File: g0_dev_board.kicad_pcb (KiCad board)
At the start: 4 copper layers, 80 x 114 mm, 198 parts, among them J201 USB_B_Mini, J202 F103_SWD, J301 USB_B_Mini, J401 RJ45_Hanrun_HR911105A_Horizon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, J501 DM3AT-SF-PEJM5, J801 Uno_IOH, J802 Uno_IOL, J803 Uno_POWER, J804 Uno_ANALOG, J805 J_LA_L, J806 J_LA_R, Q201 MMBT3904, SW701 RESET, SW702 USER, U101 STM32G0B1CCT6, U201 USBLC6-2SC6, U202 AP7361C-33E, U203 STM32F103CBTx, U301 USBLC6-2SC6, U302 FT232RL, U401 W5500, U501 W25Q32JVSSIQ, U601 TMP100, U602 TMP100, Y101 32.768kHz CL7pF, Y201 8MHz, Y401 25MHz

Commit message: feat(pcb): prepare board for placement
- Зелёные LED остаются C2297 (InGaN), резисторы к ним 330 Ом (C17630):
  ток 0.6-2.1 мА при Vf 2.6-3.1 В. Жёлто-зелёные отклонены: по
  даташитам световая отдача на мА у них в ~10 раз ниже.
- Цепи дифпар переименованы, чтобы KiCad распознавал пары:
  J201_D+/-, STL_D+/-, FT_D+/-, RXI_P/N; шаблоны классов USB90/MDI100
  обновлены.
- Отверстия шилда H801-H804: footprint из шаблона Arduino (NPTH 3.2,
  courtyard 3.4) в проектной библиотеке g0_dev_board.pretty вместо M3
  с courtyard 6.9, конфликтовавшего с разъёмами Uno.
- Исправлена арифметика в комментарии к двухцветному LED ST-Link.
- Плата синхронизирована со схемой: паритет 0, нарушений DRC 0.
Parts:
- D203, D401, D402, D403, D404: value YELLOW-GREEN -> LED
- D302: value YELLOW-GREEN -> TX
- D303: value YELLOW-GREEN -> RX
- H801, H802, H803, H804: value MountingHole_3.2mm_M3 -> Arduino_MountingHole_3.2mm; footprint MountingHole:MountingHole_3.2mm_M3 -> g0_dev_board:Arduino_MountingHole_3.2mm
- LD701: value YELLOW-GREEN -> GREEN
- R203, R424, R425, R426, R427: value 470 -> 330
- R306, R307, R701: value 390 -> 330
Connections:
- net /ft232rl/USB_DM renamed /ft232rl/FT_D-
- net /ft232rl/USB_DP renamed /ft232rl/FT_D+
- net /st_link/DM_J1 renamed /st_link/J201_D-
- net /st_link/DP_J1 renamed /st_link/J201_D+
- net /st_link/USB_DM renamed /st_link/STL_D-
- net /st_link/USB_DP renamed /st_link/STL_D+
- net /w5500/RXNNET renamed /w5500/RXI_N
- net /w5500/RXPNET renamed /w5500/RXI_P

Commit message: feat(pcb): draft component placement
Черновая расстановка по эскизу E (контрольная точка перед ручной
правкой в GUI):
- сверху вне зоны шилда: USB J201/J301, перемычки JP801/JP101/JP201,
  J202, кнопки, светодиоды; снизу: RJ45 J401 и microSD J501 на кромке,
  светодиоды W5500;
- под шилдом: ST-Link слева сверху, FT232 справа сверху, LDO по центру
  с медью под табом, U101 в центре (сторона SPI2/USART1/SWD к W5500),
  W5500 над RJ45, флэш и подтяжки SD на шине SPI2, TMP100 у МК и у LDO;
- развязка 100n <= 1.9 мм от выводов питания, высоты под шилдом <= 8 мм,
  полосы подписей гребёнок свободны.

Взвешенная длина ratsnest уменьшена на 6.7% итерациями. DRC: 0
нарушений, паритет 0, неразведённых связей 499.
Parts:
- moved D403 286.2 mm to (114.6, 139.2), turned to 90 degrees
- moved D402 283.4 mm to (114.6, 143.1), turned to 90 degrees
- moved D401 280.7 mm to (114.6, 147.0), turned to 90 degrees
- moved R424 275.4 mm to (117.5, 143.0), turned to -90 degrees
- moved R414 265.1 mm to (122.5, 115.5)
- moved R403 264.6 mm to (126.5, 115.5)
- moved R402 258.6 mm to (127.5, 112.5), turned to 90 degrees
- moved C407 258.6 mm to (126.0, 123.5), turned to -90 degrees
- moved R413 258.4 mm to (123.5, 107.0)
- moved C410 256.4 mm to (140.7, 120.5), turned to -90 degrees
- moved R430 255.0 mm to (120.0, 142.5), turned to 90 degrees
- moved R412 252.4 mm to (125.5, 109.5)
- moved C408 251.7 mm to (137.5, 122.7)
- moved R401 251.2 mm to (130.0, 109.5)
- moved R411 250.6 mm to (124.5, 118.0)
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
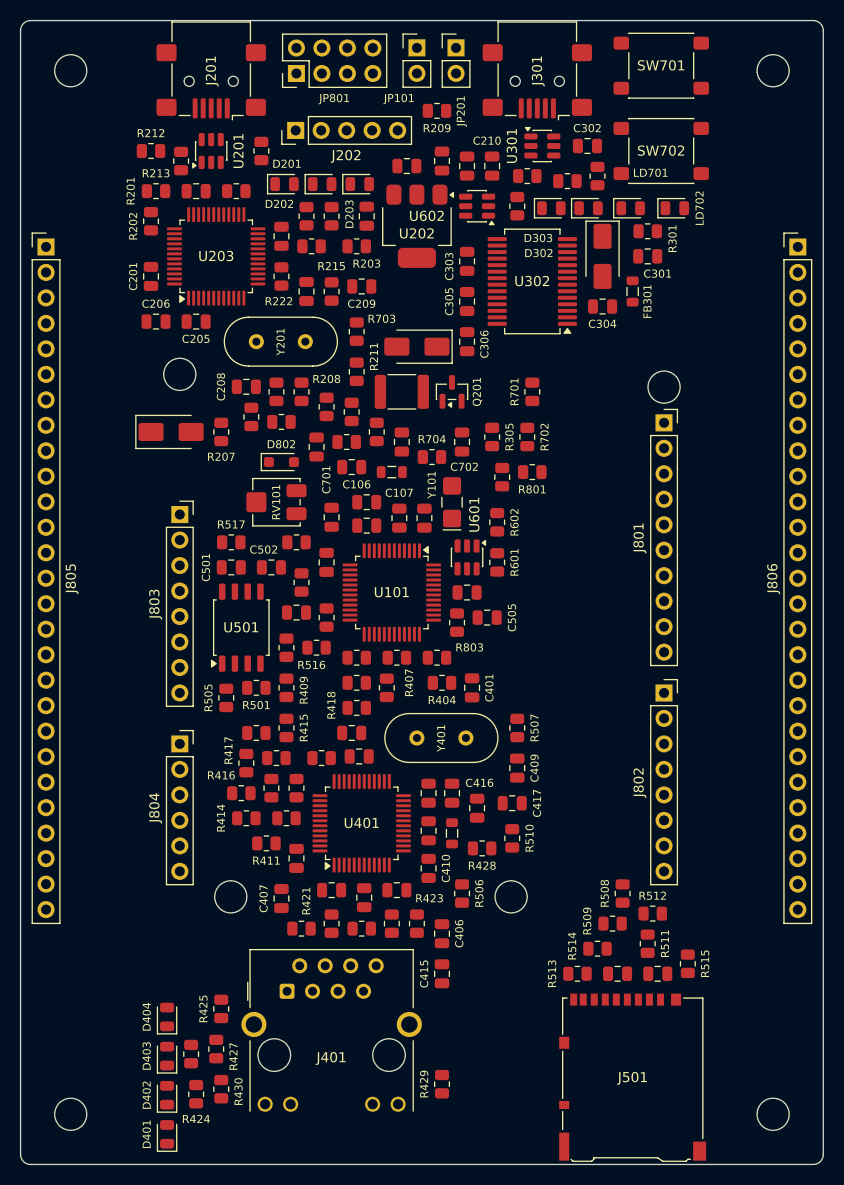
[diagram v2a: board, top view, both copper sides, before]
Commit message: feat(pcb): refine placement, add ground planes and route critical nets
Расстановка доработана: кварцы Y101/Y201/Y401 вплотную к выводам, терминация MDI
в линию между W5500 и RJ45, U203 повёрнут на 180°, флэш перенесён к microSD.
In1.Cu и In2.Cu — сплошная GND, на внешних слоях заливка GND, ~500 переходных
прошивки. Разведены и заблокированы: USB-пары (выровнены), MDI, кварцы, силовой
тракт и развязка, SPI2, USART1, SWD до JP801. DRC: 0 ошибок, паритет схемы полный,
208 неразведённых связей оставлены автотрассировщику.
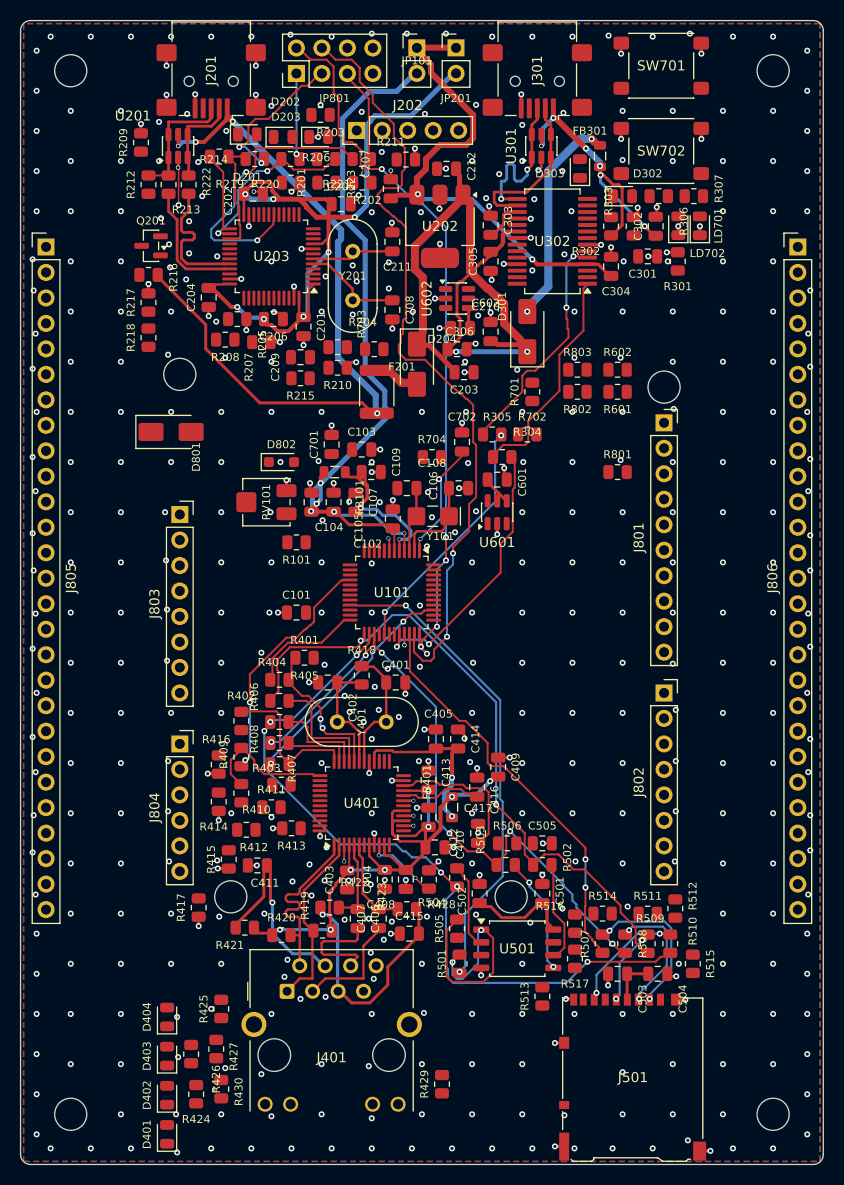
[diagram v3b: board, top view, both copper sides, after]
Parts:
- moved R517 53.8 mm to (155.2, 129.5), turned to 90 degrees
- moved C501 44.9 mm to (152.0, 123.0), turned to 90 degrees
- moved U501 42.2 mm to (149.5, 128.5), turned to 0 degrees
- moved R516 39.8 mm to (155.2, 126.0), turned to 90 degrees
- moved C502 38.6 mm to (145.8, 123.0), turned to 90 degrees
- moved R501 34.2 mm to (143.8, 130.0), turned to 90 degrees
- moved R802 33.4 mm to (155.5, 73.0), turned to 0 degrees
- moved Q201 33.3 mm to (113.0, 58.5), turned to 180 degrees
- moved R502 32.7 mm to (152.0, 120.2), turned to 0 degrees
- moved R505 32.5 mm to (143.5, 126.5)
- moved R209 29.7 mm to (112.0, 48.1), turned to 90 degrees
- moved R503 28.7 mm to (148.3, 120.2), turned to 0 degrees
- moved R803 27.9 mm to (155.5, 70.8), turned to 0 degrees
- moved R217 26.2 mm to (112.8, 64.1)
- moved R504 24.1 mm to (143.5, 121.4), turned to 90 degrees
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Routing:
- net /MCU_SWDIO: track 0.00 -> 77.7 mm, vias 0 -> 2
- net /SPI2_MISO: track 0.00 -> 73.1 mm, vias 0 -> 6
- net +3V3_MCU: track 0.00 -> 72.5 mm, vias 0 -> 5
- net /MCU_SWCLK: track 0.00 -> 71.8 mm, vias 0 -> 6
- net +3V3_STL: track 0.00 -> 70.6 mm, vias 0 -> 7
- net /st_link/VBUS_STL: track 0.00 -> 70.1 mm, vias 0 -> 4
- net +3.3V: track 0.00 -> 69.0 mm, vias 0 -> 4
- net /SPI2_SCK: track 0.00 -> 64.4 mm, vias 0 -> 2
- net /SPI2_MOSI: track 0.00 -> 61.9 mm, vias 0 -> 6
- net +5V: track 0.00 -> 61.3 mm, vias 0 -> 2
- net GND: track 0.00 -> 54.9 mm, vias 0 -> 507
- net /w5500/3V3A: track 0.00 -> 48.8 mm, vias 0 -> 8
- net /FL_CS: track 0.00 -> 47.1 mm, vias 0 -> 2
- net /SD_CS: track 0.00 -> 39.5 mm, vias 0 -> 2
- net /st_link/STL_NRST: track 0.00 -> 27.6 mm, vias 0 -> 2
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- added copper zone on B.Cu, net GND
- added copper zone on F.Cu, net GND
- added copper zone on In1.Cu, net GND
- added copper zone on In2.Cu, net GND

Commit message: refactor(pcb): remove routing and ground zones for manual re-routing
Удалены все дорожки и переходные (1555) и зоны GND на F/In1/In2/B по решению
перейти на ручную трассировку через MCP. Доработанная расстановка из 6c14ea2
сохранена. DRC: паритет со схемой полный, 499 неразведённых связей.
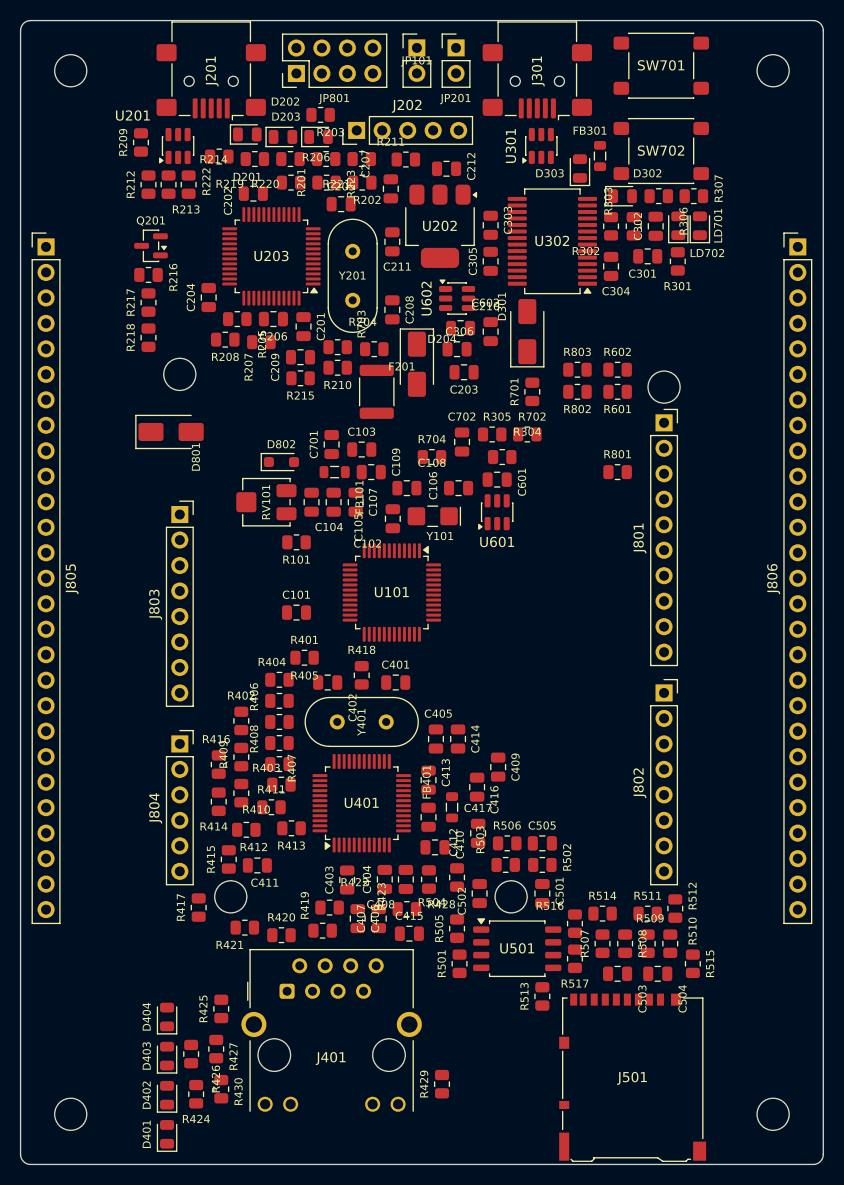
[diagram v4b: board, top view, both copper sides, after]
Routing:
- net /MCU_SWDIO: track 77.7 -> 0.00 mm, vias 2 -> 0
- net /SPI2_MISO: track 73.1 -> 0.00 mm, vias 6 -> 0
- net +3V3_MCU: track 72.5 -> 0.00 mm, vias 5 -> 0
- net /MCU_SWCLK: track 71.8 -> 0.00 mm, vias 6 -> 0
- net +3V3_STL: track 70.6 -> 0.00 mm, vias 7 -> 0
- net /st_link/VBUS_STL: track 70.1 -> 0.00 mm, vias 4 -> 0
- net +3.3V: track 69.0 -> 0.00 mm, vias 4 -> 0
- net /SPI2_SCK: track 64.4 -> 0.00 mm, vias 2 -> 0
- net /SPI2_MOSI: track 61.9 -> 0.00 mm, vias 6 -> 0
- net +5V: track 61.3 -> 0.00 mm, vias 2 -> 0
- net GND: track 54.9 -> 0.00 mm, vias 507 -> 0
- net /w5500/3V3A: track 48.8 -> 0.00 mm, vias 8 -> 0
- net /FL_CS: track 47.1 -> 0.00 mm, vias 2 -> 0
- net /SD_CS: track 39.5 -> 0.00 mm, vias 2 -> 0
- net /st_link/STL_NRST: track 27.6 -> 0.00 mm, vias 2 -> 0
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- removed copper zone on B.Cu, net GND
- removed copper zone on F.Cu, net GND
- removed copper zone on In1.Cu, net GND
- removed copper zone on In2.Cu, net GND

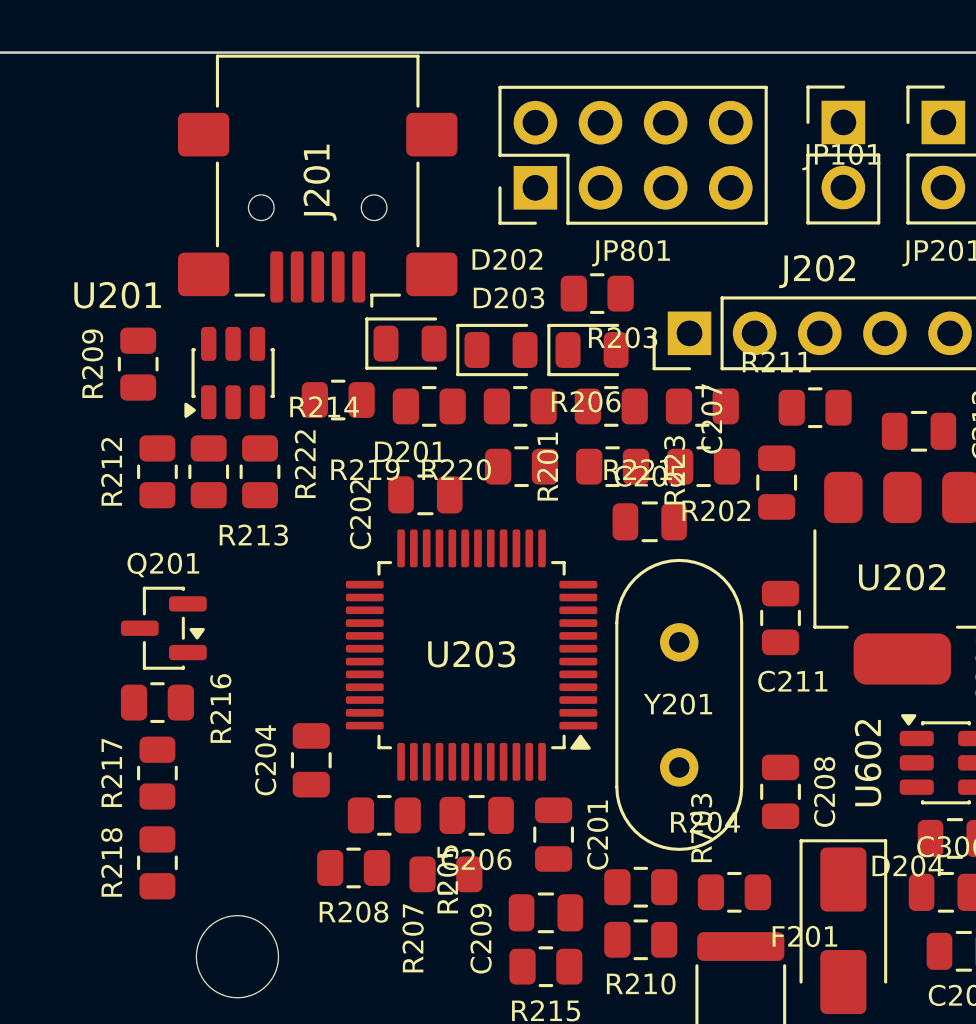
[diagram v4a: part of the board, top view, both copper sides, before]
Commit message: feat(pcb): manually route ST-Link USB, SWD and F103 escapes
Ручная трассировка через MCP: USB-пара J201 -> USBLC6 -> 0R -> F103, SWD-цепи
к JP801, верхний ряд выводов F103 (PA5, NRST, BOOT1), LED, SWO, SWD самого F103
к J202. Плоскости GND на In1/In2 восстановлены. R222 и C204 повёрнуты, C202
сдвинут на 0.4 мм ради каналов. Добавлен .kicad_dru: зазор внутри дифпар
USB 0.15 мм и MDI 0.18 мм. DRC: 0 нарушений.
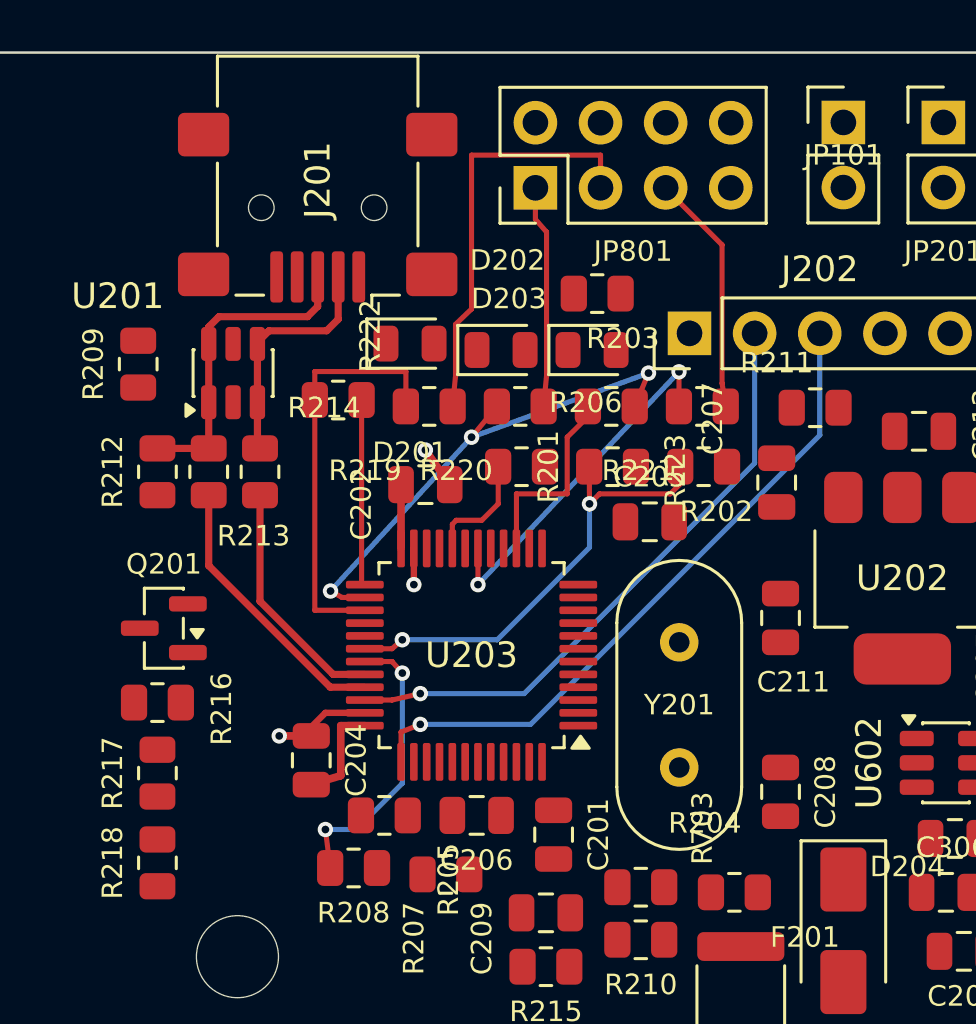
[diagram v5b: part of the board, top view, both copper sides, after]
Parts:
- moved C202 0.40 mm to (123.2, 52.9)
- turned C204 to 90 degrees
- turned R222 to 180 degrees
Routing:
- net /st_link/F103_SWCLK: track 0.00 -> 26.2 mm, vias 0 -> 1
- net /st_link/F103_SWDIO: track 0.00 -> 24.0 mm, vias 0 -> 1
- net /st_link/STL_SWCLK: track 0.00 -> 19.8 mm, vias 0 -> 3
- net /st_link/LED_STLINK: track 0.00 -> 18.1 mm, vias 0 -> 2
- net /STL_SWDIO: track 0.00 -> 16.4 mm
- net /st_link/STL_SWDIO: track 0.00 -> 16.2 mm
- net /st_link/STL_NRST: track 0.00 -> 14.2 mm, vias 0 -> 2
- net /st_link/J201_D+: track 0.00 -> 12.5 mm
- net /st_link/STL_SWO_IN: track 0.00 -> 11.2 mm, vias 0 -> 2
- net /st_link/STL_D+: track 0.00 -> 10.8 mm
- net /STL_RESET: track 0.00 -> 9.42 mm
- net /st_link/STL_D-: track 0.00 -> 9.41 mm
- net /st_link/J201_D-: track 0.00 -> 9.32 mm
- net /STL_SWCLK: track 0.00 -> 8.69 mm
- net /st_link/STL_PA5: track 0.00 -> 7.86 mm
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- added copper zone on In1.Cu, net GND
- added copper zone on In2.Cu, net GND

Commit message: feat(pcb): route F103 periphery and +3V3_STL distribution
Разведены правая и нижняя стороны F103: кварц 8 МГц, NRST к J202 и RC-цепи,
T_VCC, PC13, BOOT0, USB_RENUM, развязка. Магистраль +3V3_STL на B.Cu:
JP201 -> J202.1 -> D201/C202 и обход справа к C205/C201/R204/R215, ветка к
Q201/C204. Q201 разведён. C206 перенесён в карман у J202 (у вывода 48 не было
подхода), R205/R215 повёрнуты. GND-переходные у пассивов ST-Link. DRC: 0.
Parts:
- moved C206 26.2 mm to (146.5, 50.5), turned to 90 degrees
- turned R205 to 180 degrees
- turned R215 to 180 degrees
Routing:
- net +3V3_STL: track 6.58 -> 129.1 mm, vias 0 -> 6
- net /st_link/F103_NRST: track 0.00 -> 34.3 mm, vias 0 -> 2
- net GND: track 6.98 -> 35.6 mm, vias 3 -> 27
- net /st_link/T_VCC: track 0.00 -> 16.4 mm, vias 0 -> 2
- net /st_link/PC13: track 0.00 -> 16.3 mm, vias 0 -> 2
- net Net-(Q201-B): track 0.00 -> 13.1 mm
- net /st_link/USB_RENUM: track 0.00 -> 12.5 mm, vias 0 -> 2
- net /st_link/OSC_IN: track 0.00 -> 11.0 mm
- net /st_link/OSC_OUT: track 0.00 -> 8.35 mm
- net Net-(Q201-E): track 0.00 -> 4.73 mm
- net /st_link/BOOT_0: track 0.00 -> 4.18 mm
- net /st_link/F103_SWCLK: track 26.2 -> 23.8 mm
- net /st_link/F103_SWDIO: track 24.0 -> 21.8 mm
- net /st_link/LED_STLINK: track 18.1 -> 17.1 mm
